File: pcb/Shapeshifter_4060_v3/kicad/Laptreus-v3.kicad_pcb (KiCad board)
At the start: 2 copper layers, 285 x 94.6 mm, 109 parts, among them SW1 TAB, SW10 O, SW11 P, SW12 BKSP, SW13 ESC, SW14 A, SW15 S, SW16 D, SW17 F, SW18 G, SW19 H, SW2 Q, SW20 J, SW21 K, SW22 L, SW23 ;, SW24 ENTER, SW25 SHIFT, SW26 Z, SW27 X, SW28 C, SW29 V, SW3 W, SW30 B, SW31 N, SW32 M, SW33 ,, SW34 ., SW35 /, SW36 SHIFT, SW37 CTRL/ESC, SW38 ALT/GRV, SW39 CMD, SW4 E, SW40 FN1, SW41 SHIFT, SW42 BKSP, SW43 ENTER, SW44 SPACE, SW45 LEFT, SW46 DOWN, SW47 UP, SW48 RIGHT, SW5 R, SW6 T, SW7 Y, SW8 U, SW9 I, U1 nice_nano

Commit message: Finished board. Wow. So much faster this time...
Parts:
- SW25, SW36: footprint Kitsune-Footprints:Hybrid_Kailh_MX_Choc_Socket_Through_Hole_With_Diode -> Kitsune-Footprints:Hybrid_Kailh_MX_Choc_Socket_Through_Hole_With_Diode_No_Diode_Trace
- moved D36 0.18 mm to (8.05, 84.3)
- moved SW25 0.10 mm to (278.9, 85.1)
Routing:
- net GND: track 89.5 -> 134.1 mm, vias 0 -> 8
- net Net-(D36-Pad1): track 0.00 -> 24.8 mm
- net Net-(D25-Pad1): track 0.00 -> 21.7 mm
- added copper zone on B.Cu, net GND
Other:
- board text added: "Kitsune Keyboards Shapeshifter 4060 v3.0 by vosechu"
- board text removed: "Kitsune Keyboards Shapeshifter 4060 v3.0"
- board text removed: "by vosechu"

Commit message: Add pins for reset, add gerbers from last order, enlarged battery box
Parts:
- added JP5: Conn_01x01, Kitsune-Footprints:1X01-CLEANBIG, F.Cu at (142.8, 42.9)
- added JP6: Conn_01x01, Kitsune-Footprints:1X01-CLEANBIG, F.Cu at (152.3, 42.9)
- moved BOARD1 0.25 mm to (147.8, 84.3)
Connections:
- U1 pad 24: Net-(U1-Pad24) -> (no net)
- U1 pad 31: Net-(U1-Pad31) -> (no net)
- U1 pad 32: Net-(U1-Pad32) -> (no net)
- U1 pad 33: Net-(U1-Pad33) -> (no net)
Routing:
- net GND: track 134.1 -> 168.0 mm, vias 8 -> 40
- net /RESET: track 58.5 -> 64.6 mm
- net /ROW0: track 354.5 -> 351.4 mm
- net /COL5: track 106.6 -> 106.0 mm
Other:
- board text added: "110mAh battery"
- board text added: "Battery hole: 39mm wide x 23.5mm high"
- board text added: "Not for battery!"
- board text added: "Random USBC cable"
- board text removed: "1Ah Battery Hole (51x34x5.9mm)"

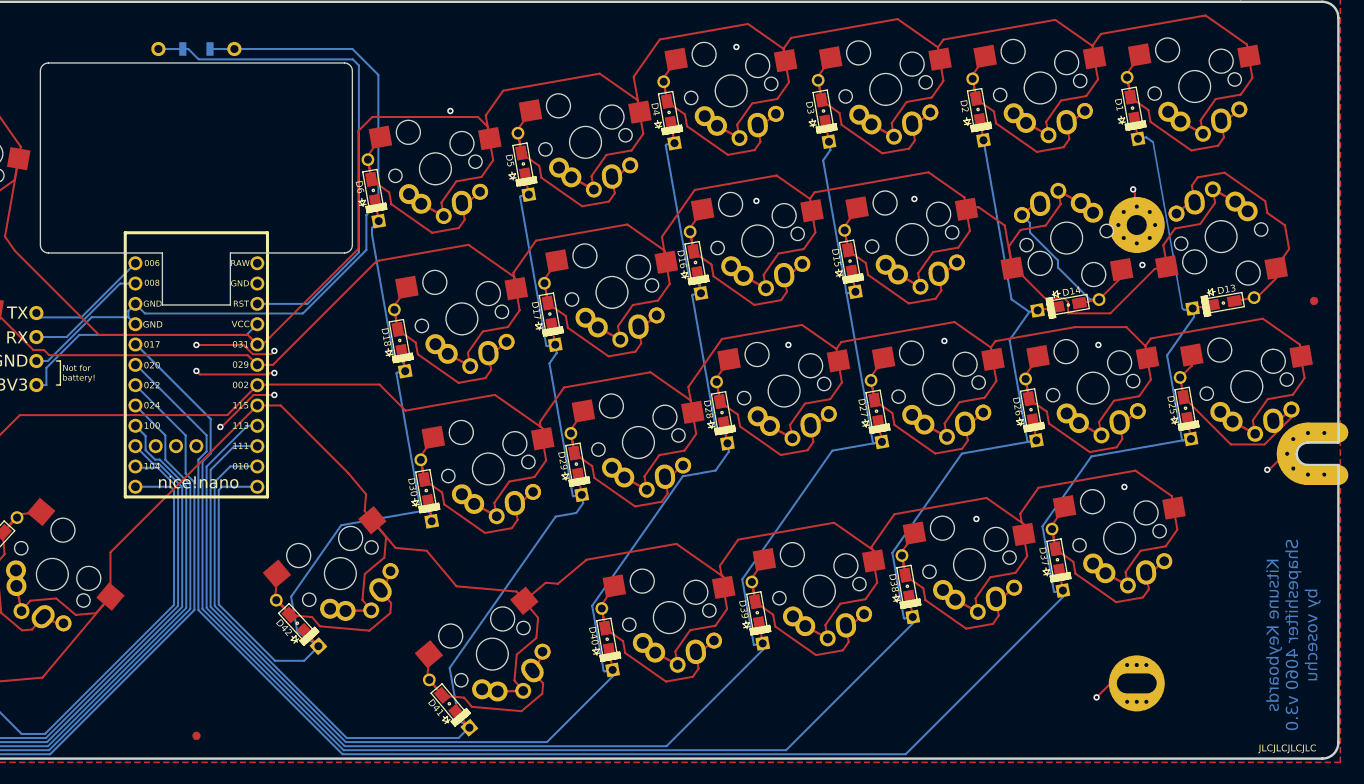
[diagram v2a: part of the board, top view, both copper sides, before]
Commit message: enlarge the flipped arduino hole
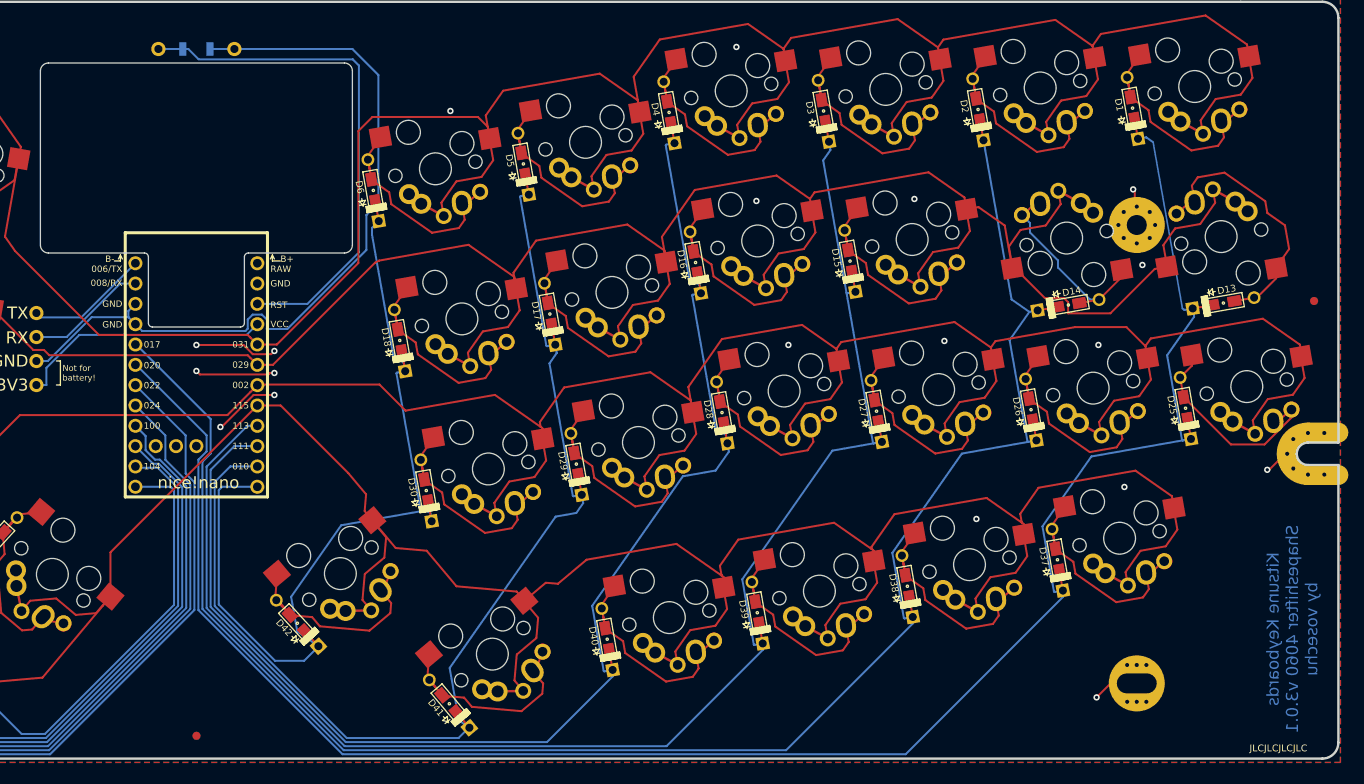
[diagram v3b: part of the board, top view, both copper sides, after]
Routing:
- net GND: track 168.0 -> 171.6 mm
- net /ROW0: track 351.4 -> 352.5 mm
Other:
- board text added: "B+"
- board text added: "B-"
- board text added: "Kitsune Keyboards Shapeshifter 4060 v3.0.1 by vosechu"
- board text removed: "Kitsune Keyboards Shapeshifter 4060 v3.0 by vosechu"

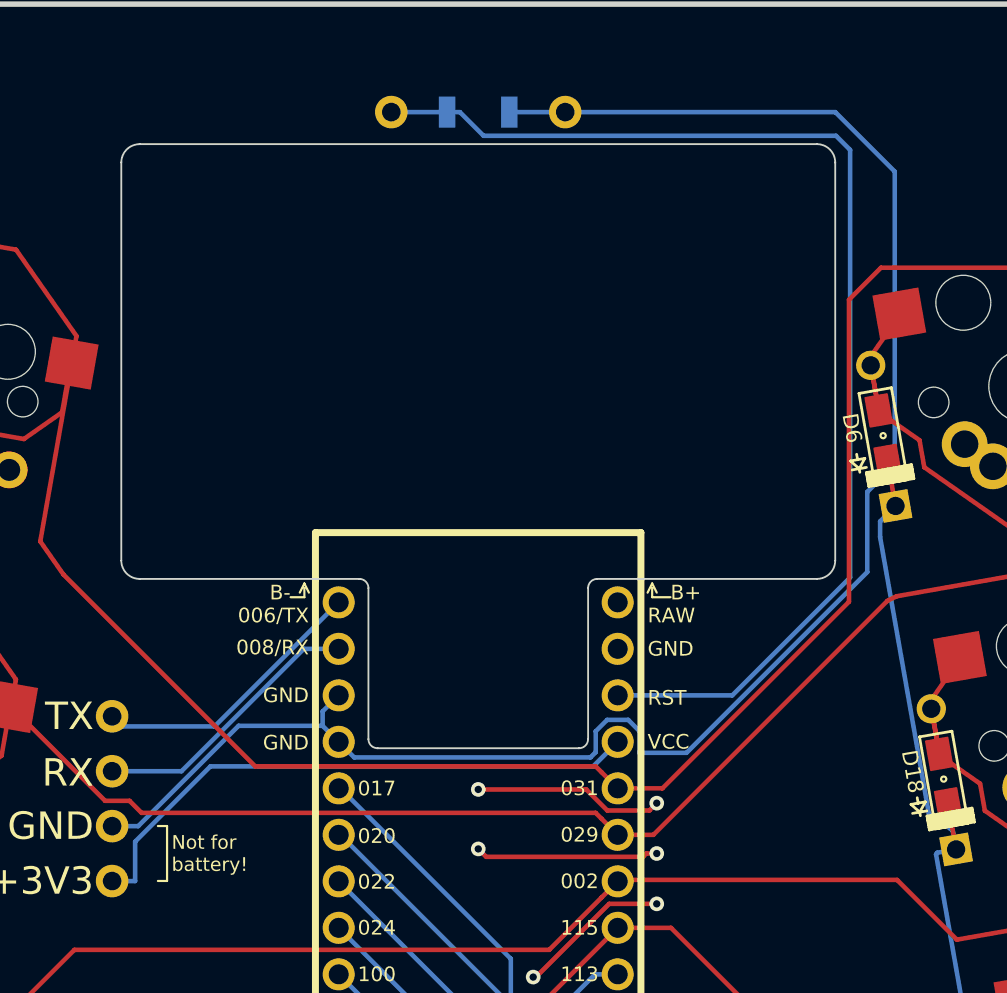
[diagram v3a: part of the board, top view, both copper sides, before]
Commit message: New revision with larger cutout for flipped pro micros
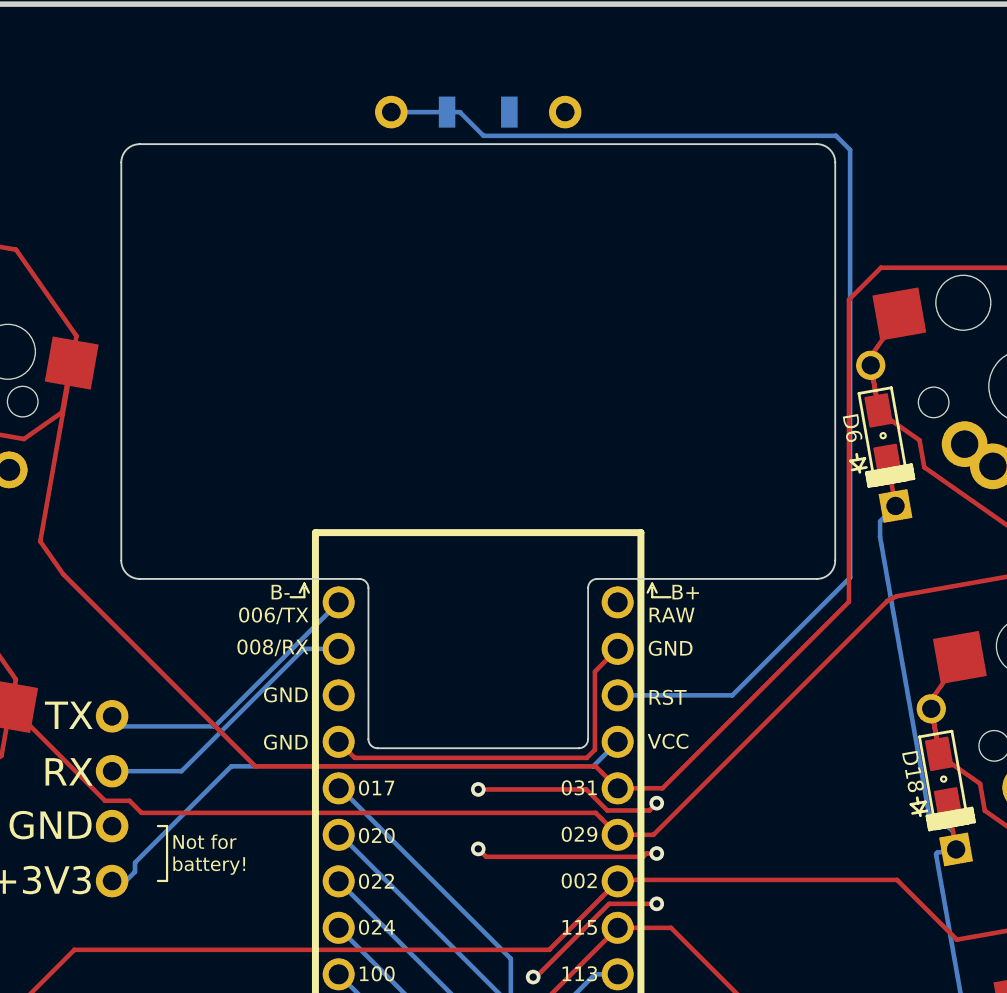
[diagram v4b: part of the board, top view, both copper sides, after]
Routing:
- net GND: track 171.6 -> 94.0 mm
- net /VCC: track 32.0 -> 31.1 mm

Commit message: Moved nice nano down, increased battery hole size
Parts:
- added ?: , , F.Cu at (176.1, -21.1)
- moved FID1 140.3 mm to (7.34, 129.5)
- moved FID2 140.3 mm to (7.34, 129.5)
- moved U1 30.0 mm to (147.3, 113.7)
- moved JP1 5.53 mm to (125.8, 81.2)
- moved JP2 5.53 mm to (125.8, 87.2)
- moved JP3 5.53 mm to (125.8, 90.2)
- moved JP4 5.53 mm to (125.8, 84.2)
- moved JP5 2.00 mm to (142.8, 40.9)
- moved JP6 2.00 mm to (152.3, 40.9)
- moved SW_RESET_1 2.00 mm to (147.6, 40.9)
- moved BOARD1 0.27 mm to (147.6, 84.4)
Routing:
- net /ROW1: track 336.3 -> 469.3 mm, vias 0 -> 11
- net /ROW0: track 352.5 -> 483.6 mm, vias 0 -> 5
- net /ROW2: track 323.3 -> 433.2 mm, vias 0 -> 10
- net GND: track 94.0 -> 46.9 mm, vias 40 -> 52
- net /ROW3: track 308.8 -> 354.4 mm, vias 0 -> 2
- net /RESET: track 64.6 -> 95.3 mm
- net /COL6: track 131.1 -> 100.5 mm
- net /COL7: track 149.3 -> 121.3 mm
- net /COL4: track 139.2 -> 111.4 mm
- net /COL3: track 164.1 -> 136.6 mm
- net /COL8: track 176.1 -> 149.3 mm
- net /COL2: track 184.7 -> 158.1 mm
- net /COL10: track 224.7 -> 198.4 mm
- net /COL9: track 197.5 -> 171.3 mm
- net /COL11: track 266.0 -> 239.8 mm
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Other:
- board text added: "500mAh battery https://www.adafruit.com/product/1578"
- board text added: "Battery hole: 39mm wide x 51mm high (30mm w/reset switch)"
- board text added: "Kitsune Keyboards Shapeshifter 4060 v3.0.2 by vosechu"
- board text added: "VCC"
- board text removed: "+3V3"
- board text removed: "Battery hole: 39mm wide x 23.5mm high"
- board text removed: "Kitsune Keyboards Shapeshifter 4060 v3.0.1 by vosechu"

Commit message: Flip reset text, flip nicenano masks
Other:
- board text added: "Kitsune Keyboards Shapeshifter 4060 v3.0.3 by vosechu"
- board text removed: "Kitsune Keyboards Shapeshifter 4060 v3.0.2 by vosechu"
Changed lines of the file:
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@@
   (module Kitsune-Footprints:nice_nano_no_Bcu_mask (layer F.Cu)
     (at 147.33 113.66 270)
-    (fp_text reference U1 (at 0 1.625 90) (layer F.SilkS) hide
+    (fp_text reference U1 (at 0 1.625 270) (layer F.SilkS) hide
       (effects (font (size 1.2 1.2) (thickness 0.2032)))
     )
-    (fp_text value nice_nano (at 0 0 90) (layer F.SilkS) hide
+    (fp_text value nice_nano (at 0 0 270) (layer F.SilkS) hide
       (effects (font (size 1.2 1.2) (thickness 0.2032)))
     )
@@
       (effects (font (size 0.8 0.8) (thickness 0.15)))
     )
-    (pad 1 thru_hole circle (at -13.97 7.62 270) (size 1.7526 1.7526) (drill 1.0922) (layers *.Cu F.SilkS F.Mask)
+    (pad 1 thru_hole circle (at -13.97 7.62 270) (size 1.7526 1.7526) (drill 1.0922) (layers *.Cu B.SilkS B.Mask)
       (net 62 /TX))
-    (pad 2 thru_hole circle (at -11.43 7.62 270) (size 1.7526 1.7526) (drill 1.0922) (layers *.Cu F.SilkS F.Mask)
+    (pad 2 thru_hole circle (at -11.43 7.62 270) (size 1.7526 1.7526) (drill 1.0922) (layers *.Cu B.SilkS B.Mask)
       (net 64 /RX))
-    (pad 3 thru_hole circle (at -8.89 7.62 270) (size 1.7526 1.7526) (drill 1.0922) (layers *.Cu F.SilkS F.Mask)
+    (pad 3 thru_hole circle (at -8.89 7.62 270) (size 1.7526 1.7526) (drill 1.0922) (layers *.Cu B.SilkS B.Mask)
       (net 1 GND))
-    (pad 4 thru_hole circle (at -6.35 7.62 270) (size 1.7526 1.7526) (drill 1.0922) (layers *.Cu F.SilkS F.Mask)
+    (pad 4 thru_hole circle (at -6.35 7.62 270) (size 1.7526 1.7526) (drill 1.0922) (layers *.Cu B.SilkS B.Mask)
       (net 1 GND))
-    (pad 5 thru_hole circle (at -3.81 7.62 270) (size 1.7526 1.7526) (drill 1.0922) (layers *.Cu F.SilkS F.Mask)
+    (pad 5 thru_hole circle (at -3.81 7.62 270) (size 1.7526 1.7526) (drill 1.0922) (layers *.Cu B.SilkS B.Mask)
       (net 5 /COL1))
-    (pad 6 thru_hole circle (at -1.27 7.62 270) (size 1.7526 1.7526) (drill 1.0922) (layers *.Cu F.SilkS F.Mask)
+    (pad 6 thru_hole circle (at -1.27 7.62 270) (size 1.7526 1.7526) (drill 1.0922) (layers *.Cu B.SilkS B.Mask)
       (net 3 /COL0))
-    (pad 7 thru_hole circle (at 1.27 7.62 270) (size 1.7526 1.7526) (drill 1.0922) (layers *.Cu F.SilkS F.Mask)
+    (pad 7 thru_hole circle (at 1.27 7.62 270) (size 1.7526 1.7526) (drill 1.0922) (layers *.Cu B.SilkS B.Mask)
       (net 25 /COL11))
-    (pad 8 thru_hole circle (at 3.81 7.62 270) (size 1.7526 1.7526) (drill 1.0922) (layers *.Cu F.SilkS F.Mask)
+    (pad 8 thru_hole circle (at 3.81 7.62 270) (size 1.7526 1.7526) (drill 1.0922) (layers *.Cu B.SilkS B.Mask)
       (net 23 /COL10))
-    (pad 9 thru_hole circle (at 6.35 7.62 270) (size 1.7526 1.7526) (drill 1.0922) (layers *.Cu F.SilkS F.Mask)
+    (pad 9 thru_hole circle (at 6.35 7.62 270) (size 1.7526 1.7526) (drill 1.0922) (layers *.Cu B.SilkS B.Mask)
       (net 21 /COL9))
-    (pad 10 thru_hole circle (at 8.89 7.62 270) (size 1.7526 1.7526) (drill 1.0922) (layers *.Cu F.SilkS F.Mask)
+    (pad 10 thru_hole circle (at 8.89 7.62 270) (size 1.7526 1.7526) (drill 1.0922) (layers *.Cu B.SilkS B.Mask)
       (net 19 /COL8))
-    (pad 11 thru_hole circle (at 11.43 7.62 270) (size 1.7526 1.7526) (drill 1.0922) (layers *.Cu F.SilkS F.Mask)
+    (pad 11 thru_hole circle (at 11.43 7.62 270) (size 1.7526 1.7526) (drill 1.0922) (layers *.Cu B.SilkS B.Mask)
       (net 17 /COL7))
-    (pad 13 thru_hole circle (at 13.97 -7.62 270) (size 1.7526 1.7526) (drill 1.0922) (layers *.Cu F.SilkS F.Mask)
+    (pad 13 thru_hole circle (at 13.97 -7.62 270) (size 1.7526 1.7526) (drill 1.0922) (layers *.Cu B.SilkS B.Mask)
       (net 13 /COL5))
-    (pad 14 thru_hole circle (at 11.43 -7.62 270) (size 1.7526 1.7526) (drill 1.0922) (layers *.Cu F.SilkS F.Mask)
+    (pad 14 thru_hole circle (at 11.43 -7.62 270) (size 1.7526 1.7526) (drill 1.0922) (layers *.Cu B.SilkS B.Mask)
       (net 11 /COL4))
-    (pad 15 thru_hole circle (at 8.89 -7.62 270) (size 1.7526 1.7526) (drill 1.0922) (layers *.Cu F.SilkS F.Mask)
+    (pad 15 thru_hole circle (at 8.89 -7.62 270) (size 1.7526 1.7526) (drill 1.0922) (layers *.Cu B.SilkS B.Mask)
       (net 9 /COL3))
-    (pad 16 thru_hole circle (at 6.35 -7.62 270) (size 1.7526 1.7526) (drill 1.0922) (layers *.Cu F.SilkS F.Mask)
+    (pad 16 thru_hole circle (at 6.35 -7.62 270) (size 1.7526 1.7526) (drill 1.0922) (layers *.Cu B.SilkS B.Mask)
       (net 7 /COL2))
-    (pad 17 thru_hole circle (at 3.81 -7.62 270) (size 1.7526 1.7526) (drill 1.0922) (layers *.Cu F.SilkS F.Mask)
+    (pad 17 thru_hole circle (at 3.81 -7.62 270) (size 1.7526 1.7526) (drill 1.0922) (layers *.Cu B.SilkS B.Mask)
       (net 67 /ROW3))
-    (pad 18 thru_hole circle (at 1.27 -7.62 270) (size 1.7526 1.7526) (drill 1.0922) (layers *.Cu F.SilkS F.Mask)
+    (pad 18 thru_hole circle (at 1.27 -7.62 270) (size 1.7526 1.7526) (drill 1.0922) (layers *.Cu B.SilkS B.Mask)
       (net 66 /ROW2))
-    (pad 19 thru_hole circle (at -1.27 -7.62 270) (size 1.7526 1.7526) (drill 1.0922) (layers *.Cu F.SilkS F.Mask)
+    (pad 19 thru_hole circle (at -1.27 -7.62 270) (size 1.7526 1.7526) (drill 1.0922) (layers *.Cu B.SilkS B.Mask)
       (net 69 /ROW1))
-    (pad 20 thru_hole circle (at -3.81 -7.62 270) (size 1.7526 1.7526) (drill 1.0922) (layers *.Cu F.SilkS F.Mask)
+    (pad 20 thru_hole circle (at -3.81 -7.62 270) (size 1.7526 1.7526) (drill 1.0922) (layers *.Cu B.SilkS B.Mask)
       (net 65 /ROW0))
-    (pad 21 thru_hole circle (at -6.35 -7.62 270) (size 1.7526 1.7526) (drill 1.0922) (layers *.Cu F.SilkS F.Mask)
+    (pad 21 thru_hole circle (at -6.35 -7.62 270) (size 1.7526 1.7526) (drill 1.0922) (layers *.Cu B.SilkS B.Mask)
       (net 63 /VCC))
-    (pad 22 thru_hole circle (at -8.89 -7.62 270) (size 1.7526 1.7526) (drill 1.0922) (layers *.Cu F.SilkS F.Mask)
+    (pad 22 thru_hole circle (at -8.89 -7.62 270) (size 1.7526 1.7526) (drill 1.0922) (layers *.Cu B.SilkS B.Mask)
       (net 68 /RESET))
-    (pad 23 thru_hole circle (at -11.43 -7.62 270) (size 1.7526 1.7526) (drill 1.0922) (layers *.Cu F.SilkS F.Mask)
+    (pad 23 thru_hole circle (at -11.43 -7.62 270) (size 1.7526 1.7526) (drill 1.0922) (layers *.Cu B.SilkS B.Mask)
       (net 1 GND))
-    (pad 12 thru_hole circle (at 13.97 7.62 270) (size 1.7526 1.7526) (drill 1.0922) (layers *.Cu F.SilkS F.Mask)
+    (pad 12 thru_hole circle (at 13.97 7.62 270) (size 1.7526 1.7526) (drill 1.0922) (layers *.Cu B.SilkS B.Mask)
       (net 15 /COL6))
-    (pad 24 thru_hole circle (at -13.97 -7.62 270) (size 1.7526 1.7526) (drill 1.0922) (layers *.Cu F.SilkS F.Mask))
+    (pad 24 thru_hole circle (at -13.97 -7.62 270) (size 1.7526 1.7526) (drill 1.0922) (layers *.Cu B.SilkS B.Mask))
     (model /Users/danny/Documents/proj/custom-keyboard/kicad-libs/3d_models/ArduinoProMicro.wrl
       (offset (xyz -13.96999979019165 -7.619999885559082 -5.841999912261963))
@@
     )
     (fp_text value RESET (at 0 -2.5) (layer B.SilkS)
-      (effects (font (size 1 1) (thickness 0.15)))
+      (effects (font (size 1 1) (thickness 0.15)) (justify mirror))
     )
     (fp_circle (center 0 0) (end 0.75 0) (layer B.Fab) (width 0.15))
@@
     (effects (font (size 0.85 0.85) (thickness 0.15)))
   )
-  (gr_text "Kitsune Keyboards\nShapeshifter 4060 v3.0.2\nby vosechu" (at 284.58 115.41 90) (layer B.Cu)
+  (gr_text "Kitsune Keyboards\nShapeshifter 4060 v3.0.3\nby vosechu" (at 284.58 115.41 90) (layer B.Cu)
     (effects (font (size 1.5 1.5) (thickness 0.3)) (justify mirror))
   )
